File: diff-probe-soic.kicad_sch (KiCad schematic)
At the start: 32 parts, among them J1 Conn_01x02, J2 Conn_Coaxial, J3 Conn_01x03, U1 LTC6228xS8, U2 LTC6228xS8, U3 LTC6228xS8

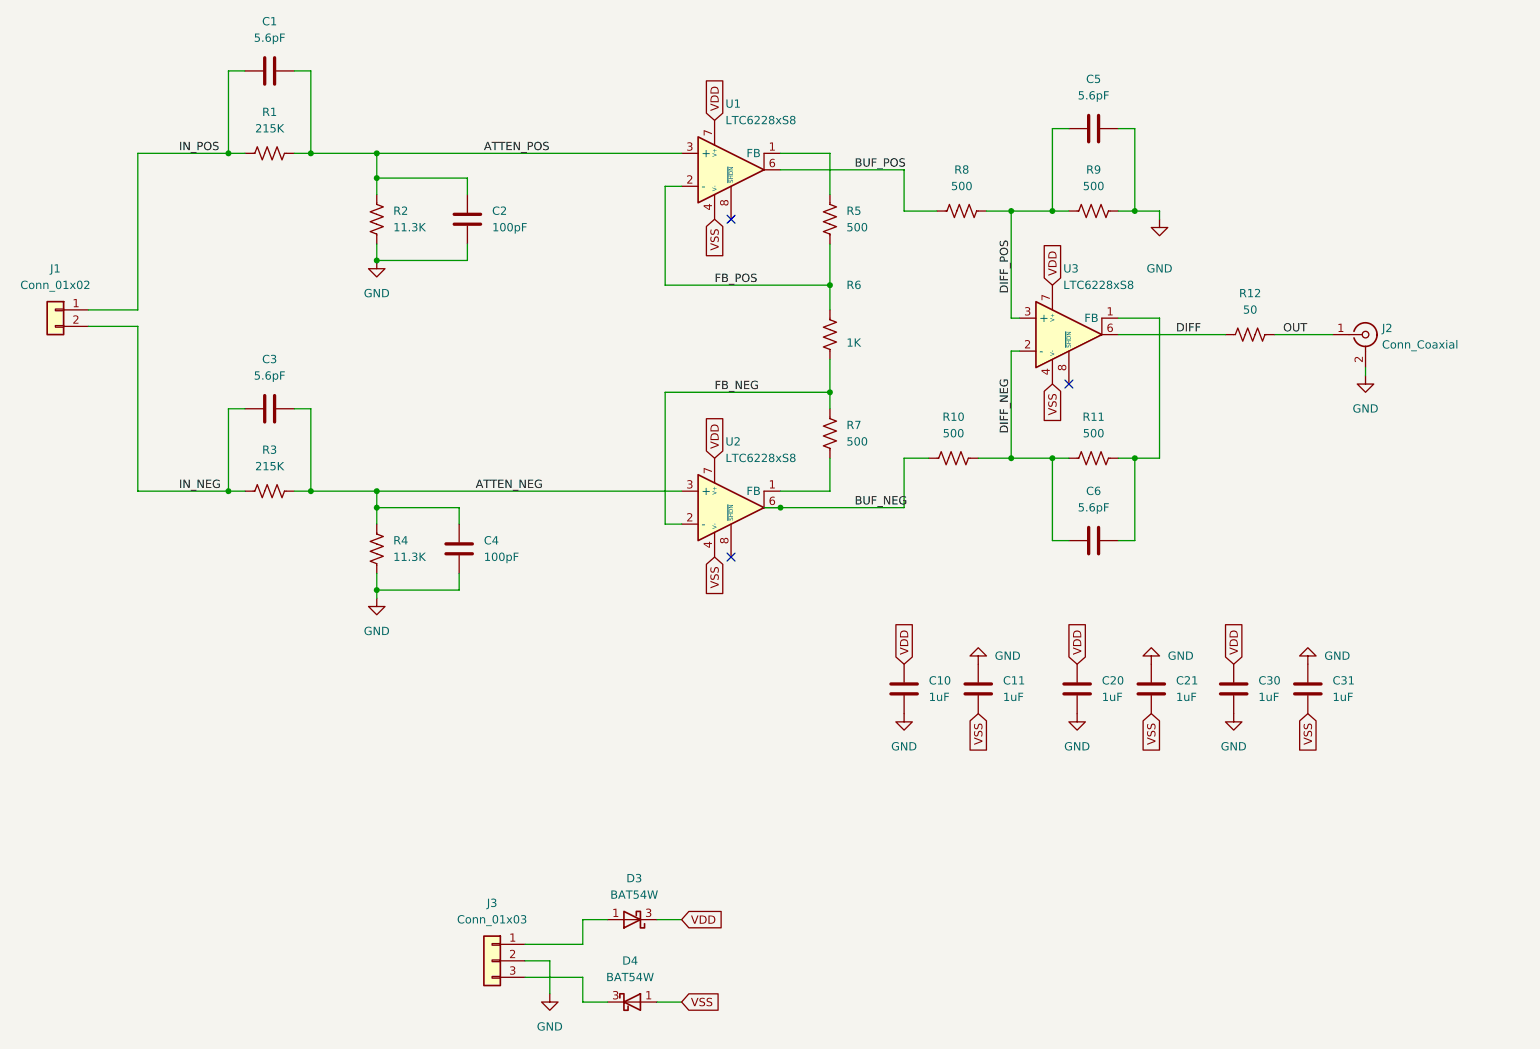
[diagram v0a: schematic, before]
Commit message: Fixed BNC connector, Moved power connector to east edge on back side.
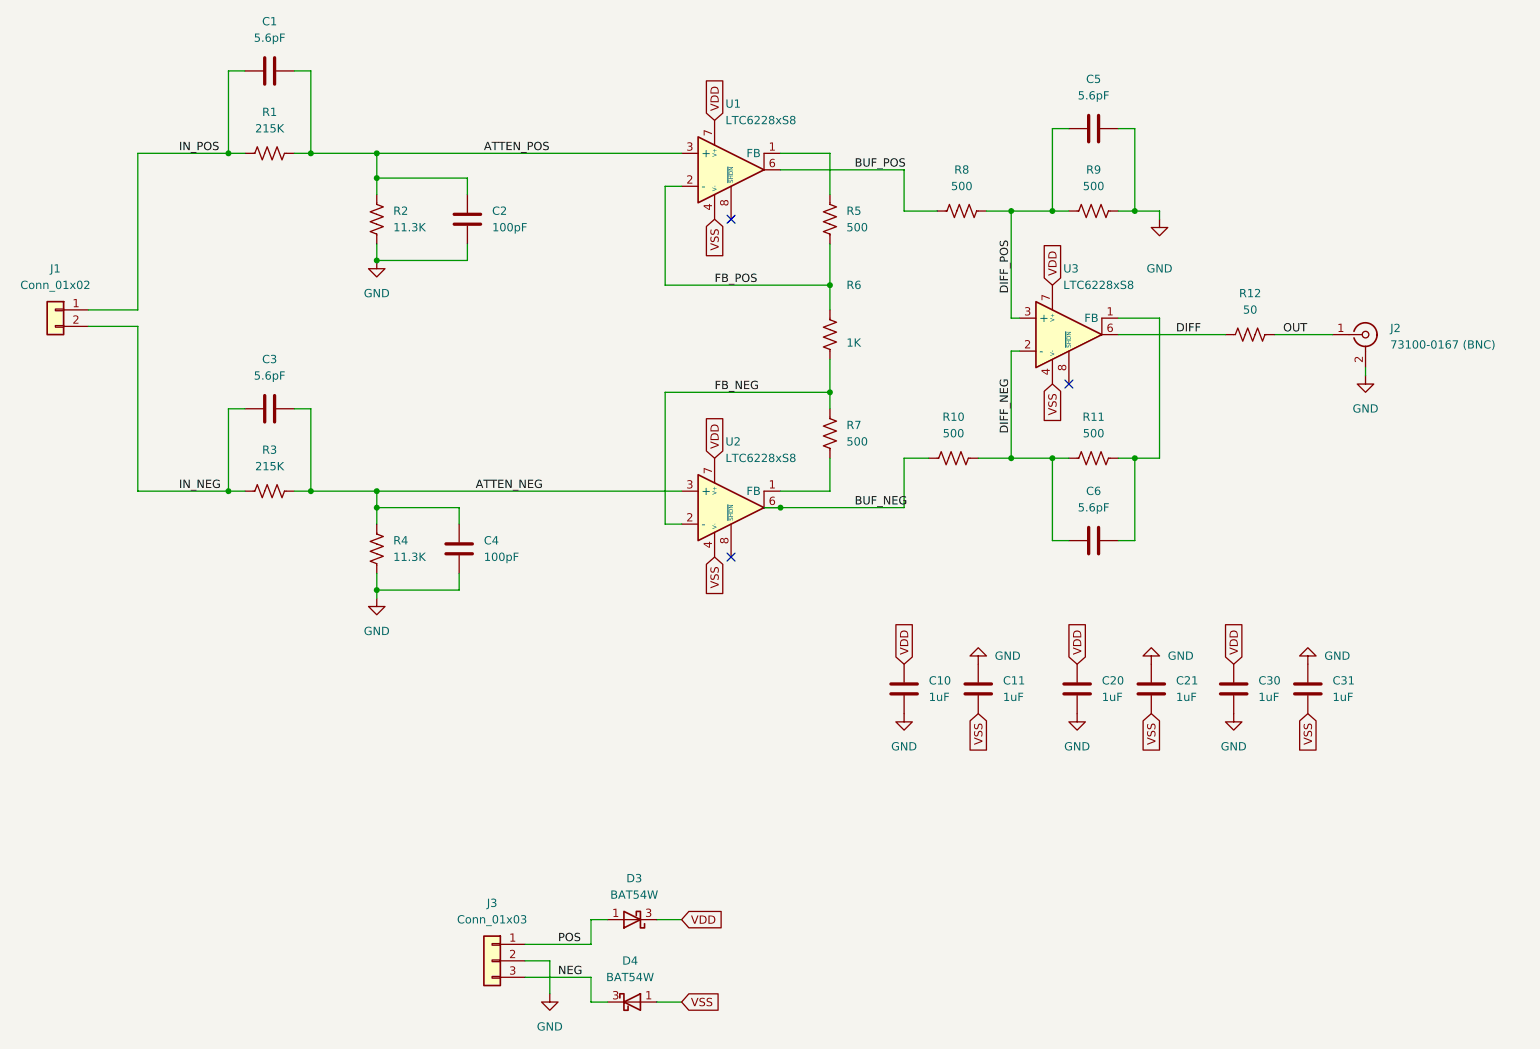
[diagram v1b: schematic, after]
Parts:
- J2: value Conn_Coaxial -> 73100-0167 (BNC); footprint Connector_Coaxial:BNC_Amphenol_031-6575_Horizontal -> $MyFootprints:BNC_Molex_73100-0167_Horizontal
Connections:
- net POS: now reaches D3.1 (A), J3.1 (Pin_1)
- net NEG: now reaches D4.3 (K), J3.3 (Pin_3)
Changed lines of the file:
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@@
     (stroke (width 0) (type default) (color 0 0 0 0))
   )
-  (wire (pts (xy 120.65 179.07) (xy 129.54 179.07))
+  (wire (pts (xy 120.65 179.07) (xy 130.81 179.07))
     (stroke (width 0) (type default) (color 0 0 0 0))
   )
@@
     (stroke (width 0) (type default) (color 0 0 0 0))
   )
-  (wire (pts (xy 129.54 184.15) (xy 129.54 187.96))
+  (wire (pts (xy 130.81 184.15) (xy 130.81 187.96))
     (stroke (width 0) (type default) (color 0 0 0 0))
   )
@@
     (stroke (width 0) (type default) (color 0 0 0 0))
   )
-  (wire (pts (xy 129.54 187.96) (xy 133.35 187.96))
+  (wire (pts (xy 130.81 187.96) (xy 133.35 187.96))
     (stroke (width 0) (type default) (color 0 0 0 0))
   )
@@
     (stroke (width 0) (type default) (color 0 0 0 0))
   )
-  (wire (pts (xy 120.65 184.15) (xy 129.54 184.15))
+  (wire (pts (xy 120.65 184.15) (xy 130.81 184.15))
     (stroke (width 0) (type default) (color 0 0 0 0))
   )
@@
     (stroke (width 0) (type default) (color 0 0 0 0))
   )
-  (wire (pts (xy 129.54 179.07) (xy 129.54 175.26))
-    (stroke (width 0) (type default) (color 0 0 0 0))
-  )
-  (wire (pts (xy 129.54 175.26) (xy 133.35 175.26))
+  (wire (pts (xy 130.81 179.07) (xy 130.81 175.26))
+    (stroke (width 0) (type default) (color 0 0 0 0))
+  )
+  (wire (pts (xy 130.81 175.26) (xy 133.35 175.26))
     (stroke (width 0) (type default) (color 0 0 0 0))
   )
@@
   )
   (label "BUF_POS" (at 171.45 59.69 0)
+    (effects (font (size 1.27 1.27)) (justify left bottom))
+  )
+  (label "NEG" (at 125.73 184.15 0)
+    (effects (font (size 1.27 1.27)) (justify left bottom))
+  )
+  (label "POS" (at 125.73 179.07 0)
     (effects (font (size 1.27 1.27)) (justify left bottom))
   )
@@
   (symbol (lib_id "Connector:Conn_Coaxial") (at 250.19 85.09 0) (unit 1)
     (in_bom yes) (on_board yes) (fields_autoplaced)
-    (property "Reference" "J2" (id 0) (at 252.73 84.1131 0)
-      (effects (font (size 1.27 1.27)) (justify left))
-    )
-    (property "Value" "Conn_Coaxial" (id 1) (at 252.73 86.6531 0)
-      (effects (font (size 1.27 1.27)) (justify left))
-    )
-    (property "Footprint" "Connector_Coaxial:BNC_Amphenol_031-6575_Horizontal" (id 2) (at 250.19 85.09 0)
+    (property "Reference" "J2" (id 0) (at 254 84.1131 0)
+      (effects (font (size 1.27 1.27)) (justify left))
+    )
+    (property "Value" "73100-0167 (BNC)" (id 1) (at 254 86.6531 0)
+      (effects (font (size 1.27 1.27)) (justify left))
+    )
+    (property "Footprint" "$MyFootprints:BNC_Molex_73100-0167_Horizontal" (id 2) (at 250.19 85.09 0)
       (effects (font (size 1.27 1.27)) hide)
     )
@@
     )
     (path "/555c73ba-0f5a-4dde-98e8-a724a5db52fd"
-      (reference "J2") (unit 1) (value "Conn_Coaxial") (footprint "Connector_Coaxial:BNC_Amphenol_031-6575_Horizontal")
+      (reference "J2") (unit 1) (value "73100-0167 (BNC)") (footprint "$MyFootprints:BNC_Molex_73100-0167_Horizontal")
     )
     (path "/e15b596a-90d5-44bb-bcad-b961210ab8f3"
